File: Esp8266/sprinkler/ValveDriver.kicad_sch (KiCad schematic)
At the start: 18 parts, among them J2 Terminal Block 1729128, J3 Terminal Block 1729128, J4 Terminal Block 1729128, Q6 MMBT2222A, Q7 MMBT2222A, Q8 MMBT2222A, U6 MMBT2907A-7-F, U7 MMBT2907A-7-F, U8 MMBT2907A-7-F

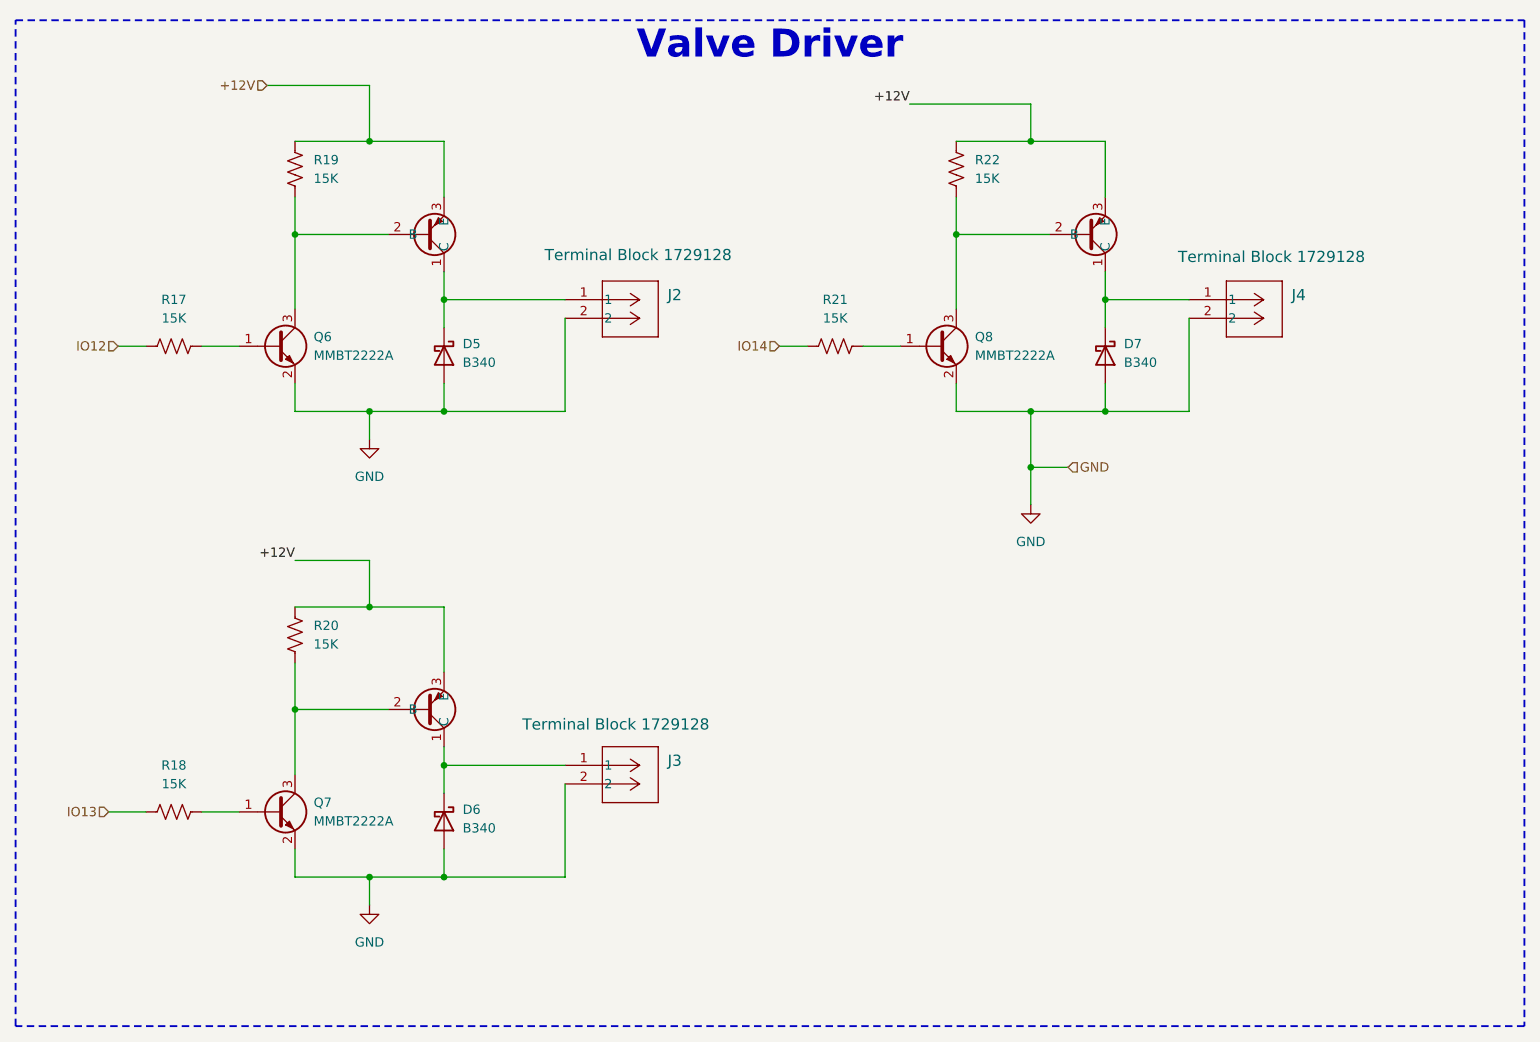
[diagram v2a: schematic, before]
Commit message: pcb
First component layout (need to verify ESP8266 board size for fitment)
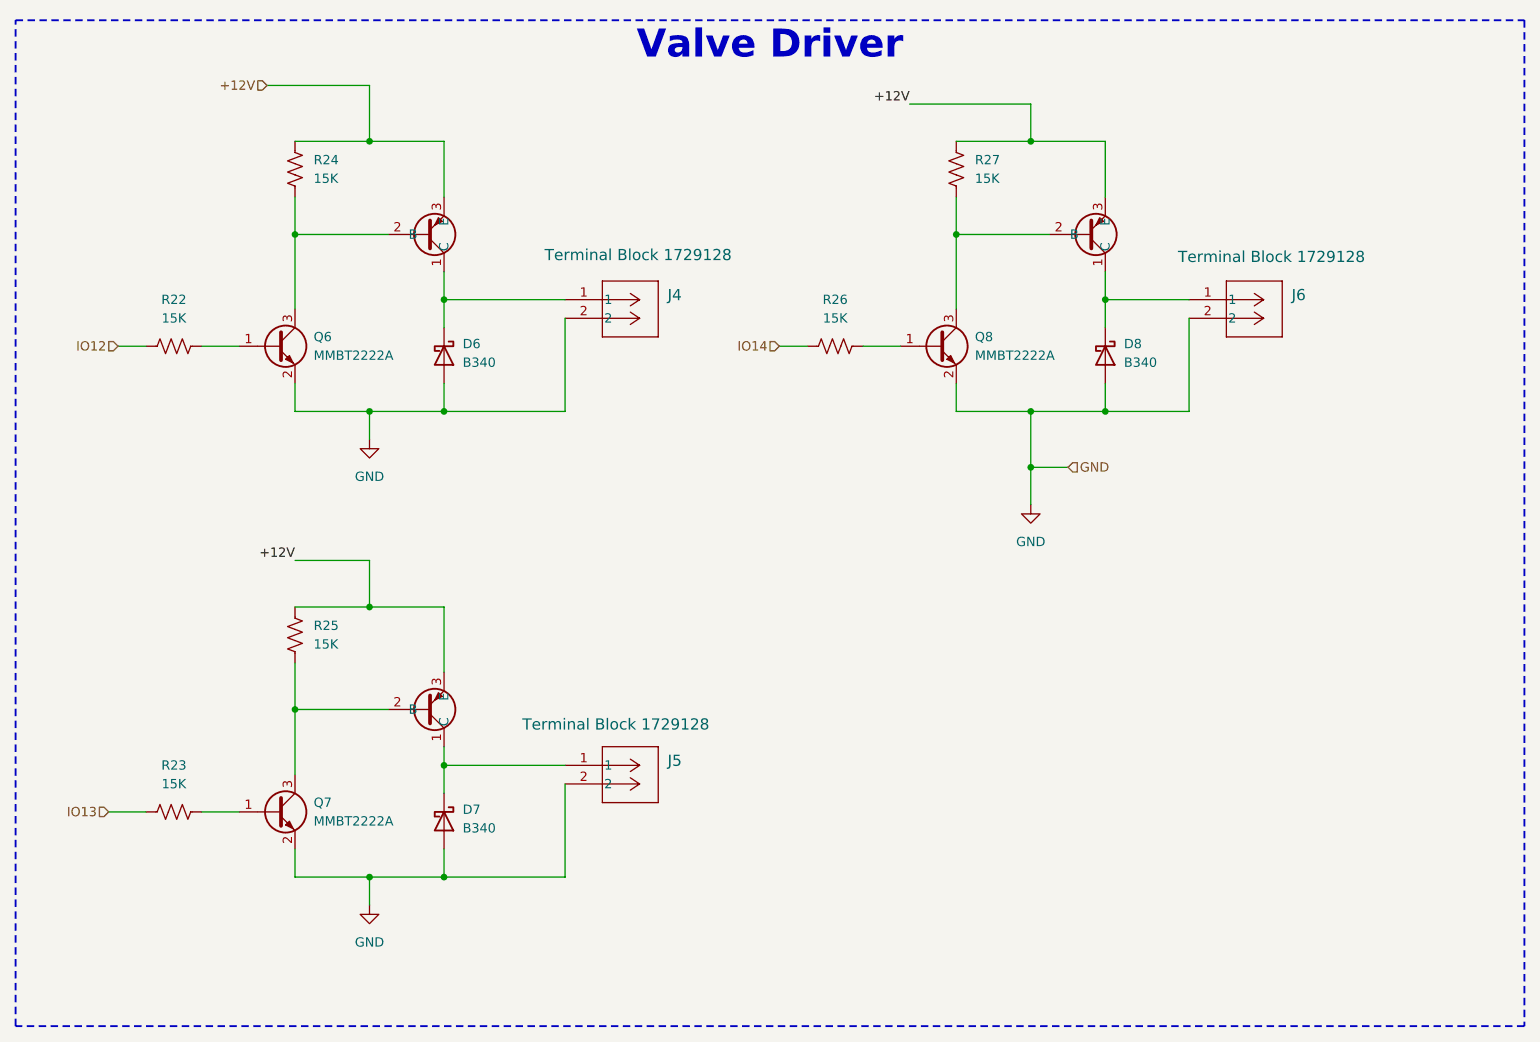
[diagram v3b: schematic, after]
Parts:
- renumbered D5 to D6, D6 to D7, D7 to D8, J2 to J4, J3 to J5, J4 to J6, R17 to R22, R18 to R23, R19 to R24, R20 to R25, R21 to R26, R22 to R27
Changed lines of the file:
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@@
 		(dnp no)
 		(fields_autoplaced yes)
-		(property "Reference" "D6"
+		(property "Reference" "D7"
 			(at 104.14 133.0325 90)
 			(effects
@@
 			(project "sprinkler"
 				(path "/00ed8740-45a2-4b9d-9104-9548b81da339/d6cea5a1-e7b3-49dc-9ebd-3b743e9b1ddf"
-					(reference "D6")
+					(reference "D7")
 					(unit 1)
 				)
@@
 		(dnp no)
 		(fields_autoplaced yes)
-		(property "Reference" "R22"
+		(property "Reference" "R27"
 			(at 173.99 44.45 0)
 			(effects
@@
 			(project "sprinkler"
 				(path "/00ed8740-45a2-4b9d-9104-9548b81da339/d6cea5a1-e7b3-49dc-9ebd-3b743e9b1ddf"
-					(reference "R22")
+					(reference "R27")
 					(unit 1)
 				)
@@
 		(dnp no)
 		(fields_autoplaced yes)
-		(property "Reference" "R18"
+		(property "Reference" "R23"
 			(at 64.77 127 90)
 			(effects
@@
 			(project "sprinkler"
 				(path "/00ed8740-45a2-4b9d-9104-9548b81da339/d6cea5a1-e7b3-49dc-9ebd-3b743e9b1ddf"
-					(reference "R18")
+					(reference "R23")
 					(unit 1)
 				)
@@
 		(on_board yes)
 		(dnp no)
-		(property "Reference" "J2"
+		(property "Reference" "J4"
 			(at 132.08 62.8649 0)
 			(effects
@@
 			(project ""
 				(path "/00ed8740-45a2-4b9d-9104-9548b81da339/d6cea5a1-e7b3-49dc-9ebd-3b743e9b1ddf"
-					(reference "J2")
+					(reference "J4")
 					(unit 1)
 				)
@@
 		(dnp no)
 		(fields_autoplaced yes)
-		(property "Reference" "#PWR026"
+		(property "Reference" "#PWR035"
 			(at 91.44 88.9 0)
 			(effects
@@
 			(project ""
 				(path "/00ed8740-45a2-4b9d-9104-9548b81da339/d6cea5a1-e7b3-49dc-9ebd-3b743e9b1ddf"
-					(reference "#PWR026")
+					(reference "#PWR035")
 					(unit 1)
 				)
@@
 		(on_board yes)
 		(dnp no)
-		(property "Reference" "J4"
+		(property "Reference" "J6"
 			(at 217.17 62.8649 0)
 			(effects
@@
 			(project ""
 				(path "/00ed8740-45a2-4b9d-9104-9548b81da339/d6cea5a1-e7b3-49dc-9ebd-3b743e9b1ddf"
-					(reference "J4")
+					(reference "J6")
 					(unit 1)
 				)
@@
 		(dnp no)
 		(fields_autoplaced yes)
-		(property "Reference" "D5"
+		(property "Reference" "D6"
 			(at 104.14 69.5325 90)
 			(effects
@@
 			(project ""
 				(path "/00ed8740-45a2-4b9d-9104-9548b81da339/d6cea5a1-e7b3-49dc-9ebd-3b743e9b1ddf"
-					(reference "D5")
+					(reference "D6")
 					(unit 1)
 				)
@@
 		(dnp no)
 		(fields_autoplaced yes)
-		(property "Reference" "#PWR028"
+		(property "Reference" "#PWR037"
 			(at 181.61 97.79 0)
 			(effects
@@
 			(project "sprinkler"
 				(path "/00ed8740-45a2-4b9d-9104-9548b81da339/d6cea5a1-e7b3-49dc-9ebd-3b743e9b1ddf"
-					(reference "#PWR028")
+					(reference "#PWR037")
 					(unit 1)
 				)
@@
 		(dnp no)
 		(fields_autoplaced yes)
-		(property "Reference" "D7"
+		(property "Reference" "D8"
 			(at 194.31 69.5325 90)
 			(effects
@@
 			(project "sprinkler"
 				(path "/00ed8740-45a2-4b9d-9104-9548b81da339/d6cea5a1-e7b3-49dc-9ebd-3b743e9b1ddf"
-					(reference "D7")
+					(reference "D8")
 					(unit 1)
 				)
@@
 		(dnp no)
 		(fields_autoplaced yes)
-		(property "Reference" "R20"
+		(property "Reference" "R25"
 			(at 83.82 107.95 0)
 			(effects
@@
 			(project "sprinkler"
 				(path "/00ed8740-45a2-4b9d-9104-9548b81da339/d6cea5a1-e7b3-49dc-9ebd-3b743e9b1ddf"
-					(reference "R20")
+					(reference "R25")
 					(unit 1)
 				)
@@
 		(on_board yes)
 		(dnp no)
-		(property "Reference" "J3"
+		(property "Reference" "J5"
 			(at 132.08 126.3649 0)
 			(effects
@@
 			(project ""
 				(path "/00ed8740-45a2-4b9d-9104-9548b81da339/d6cea5a1-e7b3-49dc-9ebd-3b743e9b1ddf"
-					(reference "J3")
+					(reference "J5")
 					(unit 1)
 				)
@@
 		(dnp no)
 		(fields_autoplaced yes)
-		(property "Reference" "R19"
+		(property "Reference" "R24"
 			(at 83.82 44.45 0)
 			(effects
@@
 			(project ""
 				(path "/00ed8740-45a2-4b9d-9104-9548b81da339/d6cea5a1-e7b3-49dc-9ebd-3b743e9b1ddf"
-					(reference "R19")
+					(reference "R24")
 					(unit 1)
 				)
@@
 		(dnp no)
 		(fields_autoplaced yes)
-		(property "Reference" "R17"
+		(property "Reference" "R22"
 			(at 64.77 63.5 90)
 			(effects
@@
 			(project ""
 				(path "/00ed8740-45a2-4b9d-9104-9548b81da339/d6cea5a1-e7b3-49dc-9ebd-3b743e9b1ddf"
-					(reference "R17")
+					(reference "R22")
 					(unit 1)
 				)
@@
 		(dnp no)
 		(fields_autoplaced yes)
-		(property "Reference" "R21"
+		(property "Reference" "R26"
 			(at 154.94 63.5 90)
 			(effects
@@
 			(project "sprinkler"
 				(path "/00ed8740-45a2-4b9d-9104-9548b81da339/d6cea5a1-e7b3-49dc-9ebd-3b743e9b1ddf"
-					(reference "R21")
+					(reference "R26")
 					(unit 1)
 				)
@@
 		(dnp no)
 		(fields_autoplaced yes)
-		(property "Reference" "#PWR027"
+		(property "Reference" "#PWR036"
 			(at 91.44 152.4 0)
 			(effects
@@
 			(project "sprinkler"
 				(path "/00ed8740-45a2-4b9d-9104-9548b81da339/d6cea5a1-e7b3-49dc-9ebd-3b743e9b1ddf"
-					(reference "#PWR027")
-					(unit 1)
-				)
+					(reference "#PWR036")
+					(unit 1)
+				)
